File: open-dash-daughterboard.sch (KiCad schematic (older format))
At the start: 0 parts

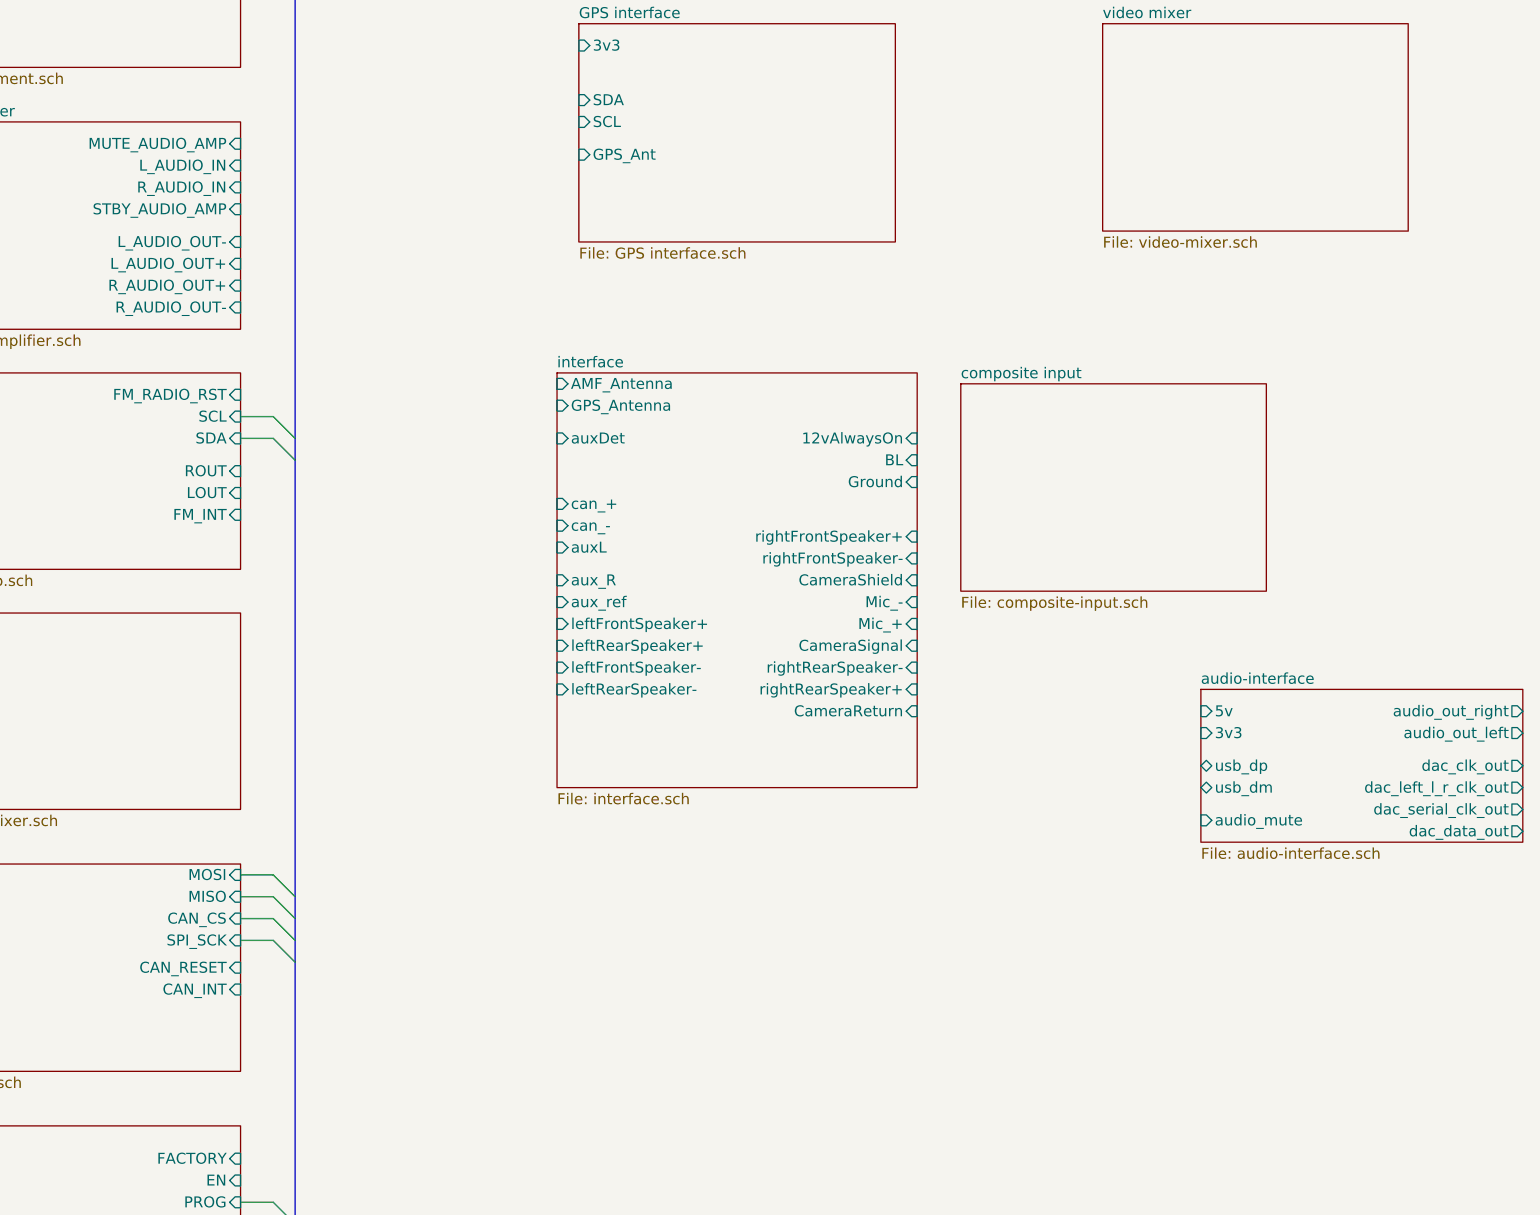
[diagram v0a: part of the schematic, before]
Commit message: Slight re-arrangment, and added datasheets for potential video options.
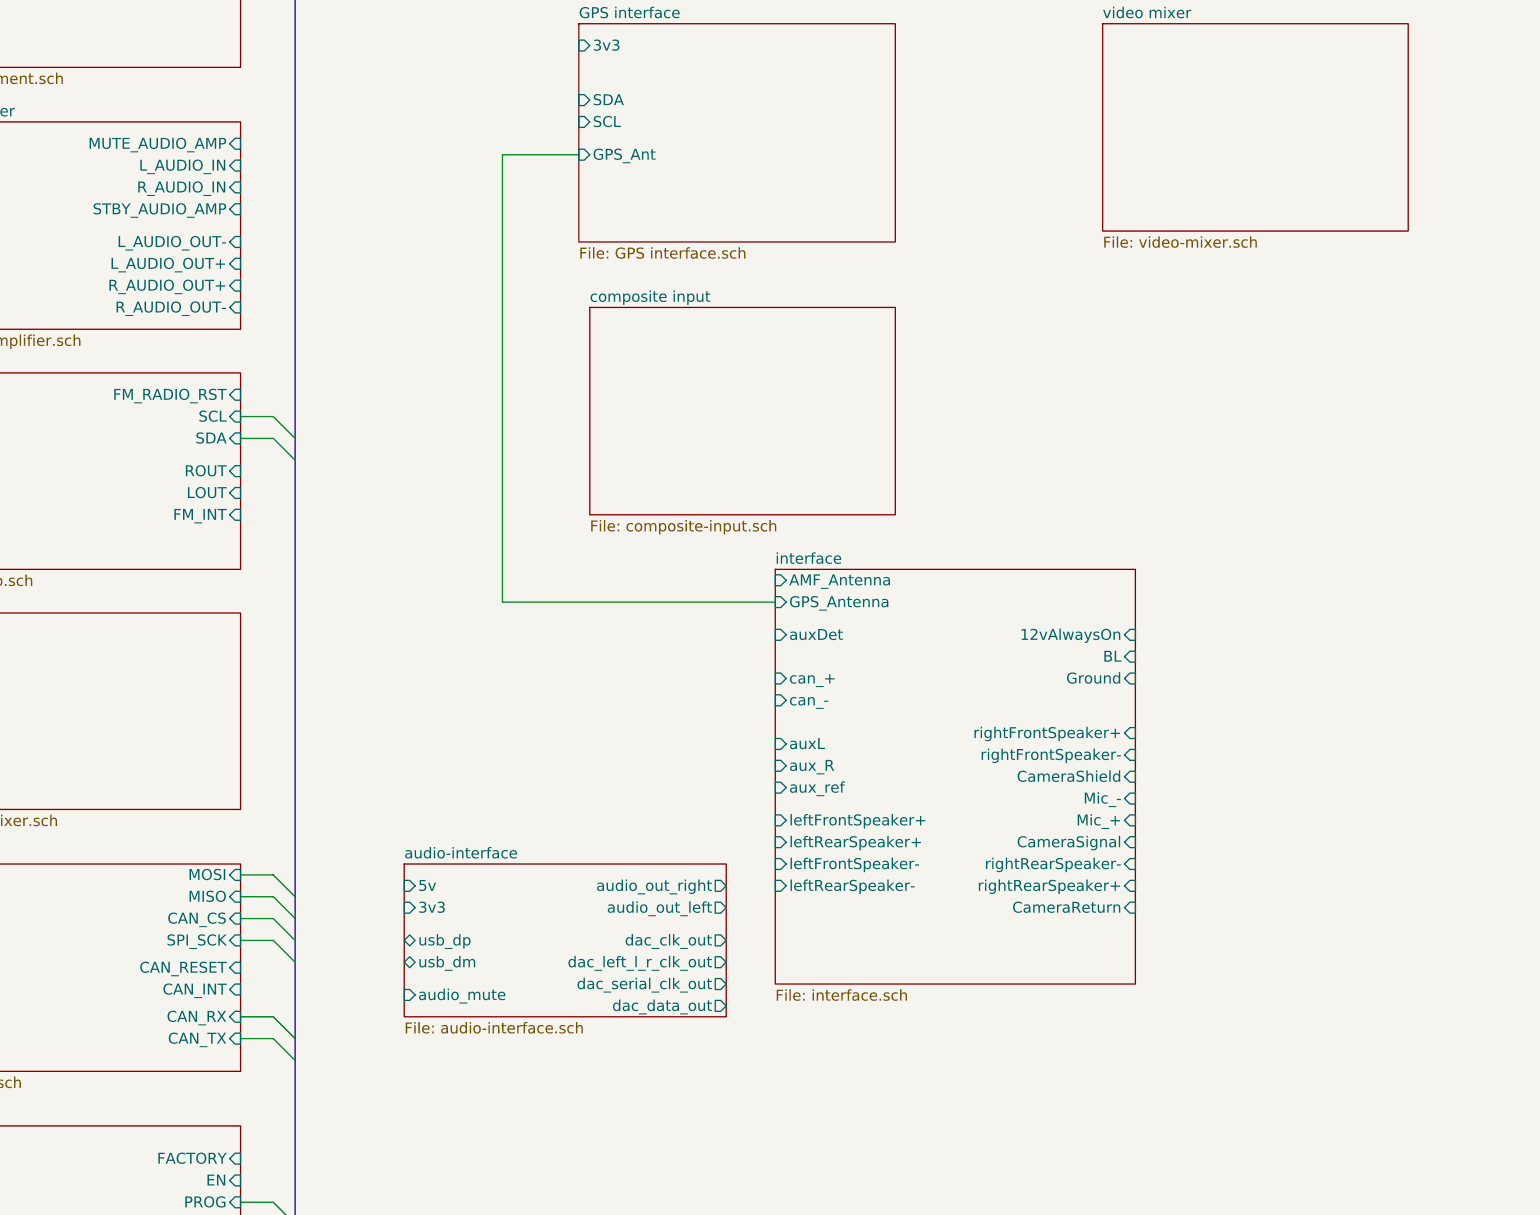
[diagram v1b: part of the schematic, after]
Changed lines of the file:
@@
 F7 "CAN_RESET" I R 4000 6375 50
 F8 "CAN_INT" I R 4000 6475 50
+F9 "CAN_RX" I R 4000 6600 50
+F10 "CAN_TX" I R 4000 6700 50
 $EndSheet
 $Sheet
@@
 $EndSheet
 $Sheet
-S 5450 3650 1650 1900
+S 6450 4550 1650 1900
 U 5ABD187E
 F0 "interface" 50
 F1 "interface.sch" 50
-F2 "AMF_Antenna" I L 5450 3700 50
-F3 "GPS_Antenna" I L 5450 3800 50
-F4 "can_+" I L 5450 4250 50
-F5 "aux_R" I L 5450 4600 50
-F6 "aux_ref" I L 5450 4700 50
-F7 "can_-" I L 5450 4350 50
-F8 "BL" I R 7100 4050 50
-F9 "Ground" I R 7100 4150 50
-F10 "Mic_-" I R 7100 4700 50
-F11 "Mic_+" I R 7100 4800 50
-F12 "CameraSignal" I R 7100 4900 50
-F13 "CameraShield" I R 7100 4600 50
-F14 "CameraReturn" I R 7100 5200 50
-F15 "12vAlwaysOn" I R 7100 3950 50
-F16 "rightRearSpeaker+" I R 7100 5100 50
-F17 "rightFrontSpeaker+" I R 7100 4400 50
-F18 "leftFrontSpeaker+" I L 5450 4800 50
-F19 "leftRearSpeaker+" I L 5450 4900 50
-F20 "rightRearSpeaker-" I R 7100 5000 50
-F21 "rightFrontSpeaker-" I R 7100 4500 50
-F22 "leftFrontSpeaker-" I L 5450 5000 50
-F23 "leftRearSpeaker-" I L 5450 5100 50
-F24 "auxDet" I L 5450 3950 50
-F25 "auxL" I L 5450 4450 50
+F2 "AMF_Antenna" I L 6450 4600 50
+F3 "GPS_Antenna" I L 6450 4700 50
+F4 "can_+" I L 6450 5050 50
+F5 "aux_R" I L 6450 5450 50
+F6 "aux_ref" I L 6450 5550 50
+F7 "can_-" I L 6450 5150 50
+F8 "BL" I R 8100 4950 50
+F9 "Ground" I R 8100 5050 50
+F10 "Mic_-" I R 8100 5600 50
+F11 "Mic_+" I R 8100 5700 50
+F12 "CameraSignal" I R 8100 5800 50
+F13 "CameraShield" I R 8100 5500 50
+F14 "CameraReturn" I R 8100 6100 50
+F15 "12vAlwaysOn" I R 8100 4850 50
+F16 "rightRearSpeaker+" I R 8100 6000 50
+F17 "rightFrontSpeaker+" I R 8100 5300 50
+F18 "leftFrontSpeaker+" I L 6450 5700 50
+F19 "leftRearSpeaker+" I L 6450 5800 50
+F20 "rightRearSpeaker-" I R 8100 5900 50
+F21 "rightFrontSpeaker-" I R 8100 5400 50
+F22 "leftFrontSpeaker-" I L 6450 5900 50
+F23 "leftRearSpeaker-" I L 6450 6000 50
+F24 "auxDet" I L 6450 4850 50
+F25 "auxL" I L 6450 5350 50
 $EndSheet
 $Sheet
@@
 $EndSheet
 $Sheet
-S 7300 3700 1400 950
+S 5600 3350 1400 950
 U 5ABE8D90
 F0 "composite input" 50
@@
 $EndSheet
 $Sheet
-S 8400 5100 1475 700
+S 4750 5900 1475 700
 U 5AE37EA7
 F0 "audio-interface" 50
 F1 "audio-interface.sch" 50
-F2 "5v" I L 8400 5200 50
-F3 "usb_dm" B L 8400 5550 50
-F4 "usb_dp" B L 8400 5450 50
-F5 "3v3" I L 8400 5300 50
-F6 "audio_mute" I L 8400 5700 50
-F7 "audio_out_right" O R 9875 5200 50
-F8 "audio_out_left" O R 9875 5300 50
-F9 "dac_clk_out" O R 9875 5450 50
-F10 "dac_data_out" O R 9875 5750 50
-F11 "dac_left_l_r_clk_out" O R 9875 5550 50
-F12 "dac_serial_clk_out" O R 9875 5650 50
-$EndSheet
+F2 "5v" I L 4750 6000 50
+F3 "usb_dm" B L 4750 6350 50
+F4 "usb_dp" B L 4750 6250 50
+F5 "3v3" I L 4750 6100 50
+F6 "audio_mute" I L 4750 6500 50
+F7 "audio_out_right" O R 6225 6000 50
+F8 "audio_out_left" O R 6225 6100 50
+F9 "dac_clk_out" O R 6225 6250 50
+F10 "dac_data_out" O R 6225 6550 50
+F11 "dac_left_l_r_clk_out" O R 6225 6350 50
+F12 "dac_serial_clk_out" O R 6225 6450 50
+$EndSheet
+Entry Wire Line
+	4150 6600 4250 6700
+Entry Wire Line
+	4150 6700 4250 6800
+Wire Wire Line
+	4150 6600 4000 6600
+Wire Wire Line
+	4000 6700 4150 6700
+Wire Wire Line
+	5550 2650 5200 2650
+Wire Wire Line
+	5200 2650 5200 4700
+Wire Wire Line
+	5200 4700 6450 4700
 Wire Bus Line
 	2300 250  2300 7500

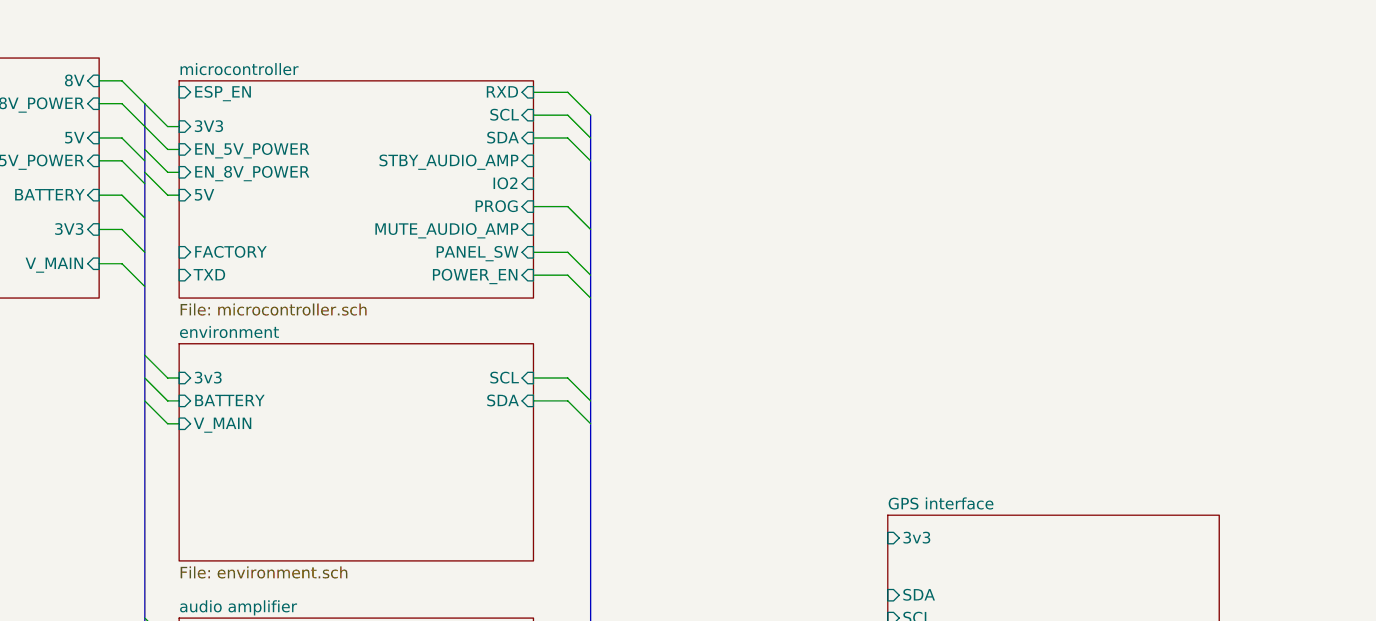
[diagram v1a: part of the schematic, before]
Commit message: added mainboard-interface
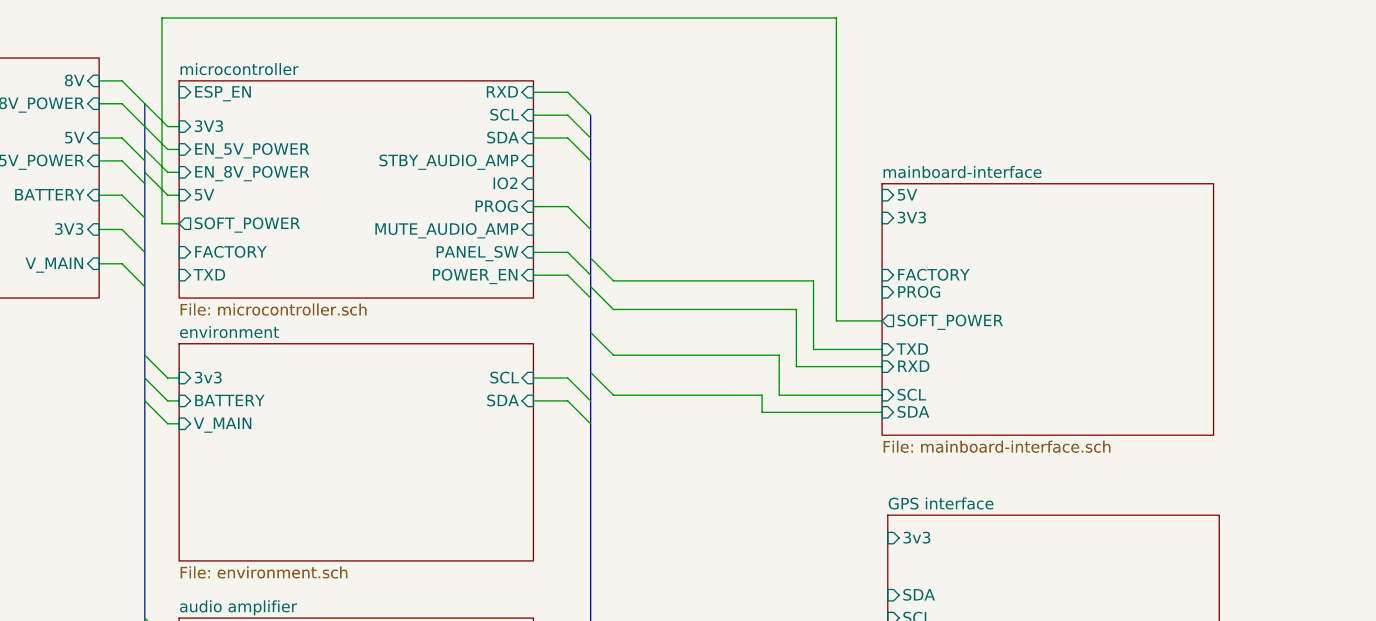
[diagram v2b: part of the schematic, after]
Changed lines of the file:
@@
 EESchema Schematic File Version 4
-LIBS:open-dash-daughterboard-cache
 EELAYER 26 0
 EELAYER END
 $Descr USLetter 11000 8500
 encoding utf-8
-Sheet 1 14
+Sheet 1 15
 Title ""
 Date ""
@@
 F16 "5V" I L 2450 650 50
 F17 "ESP_EN" I L 2450 200 50
+F18 "SOFT_POWER" O L 2450 775 50
 $EndSheet
 $Sheet
@@
 Wire Wire Line
 	5200 4700 6450 4700
+$Sheet
+S 5525 600  1450 1100
+U 5AF5E3D2
+F0 "mainboard-interface" 50
+F1 "mainboard-interface.sch" 50
+F2 "3V3" I L 5525 750 50
+F3 "PROG" I L 5525 1075 50
+F4 "FACTORY" I L 5525 1000 50
+F5 "SCL" I L 5525 1525 50
+F6 "5V" I L 5525 650 50
+F7 "TXD" I L 5525 1325 50
+F8 "RXD" I L 5525 1400 50
+F9 "SDA" I L 5525 1600 50
+F10 "SOFT_POWER" O L 5525 1200 50
+$EndSheet
+Wire Wire Line
+	2450 775  2375 775
+Wire Wire Line
+	2375 775  2375 -125
+Wire Wire Line
+	2375 -125 5325 -125
+Wire Wire Line
+	5325 -125 5325 1200
+Wire Wire Line
+	5325 1200 5525 1200
+Entry Wire Line
+	4250 925  4350 1025
+Entry Wire Line
+	4250 1050 4350 1150
+Entry Wire Line
+	4250 1250 4350 1350
+Entry Wire Line
+	4250 1425 4350 1525
+Wire Wire Line
+	5525 1325 5225 1325
+Wire Wire Line
+	5225 1325 5225 1025
+Wire Wire Line
+	5225 1025 4350 1025
+Wire Wire Line
+	5525 1400 5150 1400
+Wire Wire Line
+	5150 1400 5150 1150
+Wire Wire Line
+	5150 1150 4350 1150
+Wire Wire Line
+	5525 1525 5075 1525
+Wire Wire Line
+	5075 1525 5075 1350
+Wire Wire Line
+	5075 1350 4350 1350
+Wire Wire Line
+	5525 1600 5000 1600
+Wire Wire Line
+	5000 1600 5000 1525
+Wire Wire Line
+	5000 1525 4350 1525
 Wire Bus Line
 	2300 250  2300 7500
